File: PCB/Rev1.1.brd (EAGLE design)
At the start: 101.6 x 81.3 mm, 27 parts, among them U1 ATMEGA328P-PU, U2 BT, U3 SMD_H-BRIDGE

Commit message: Minor Board Changes
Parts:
- moved C5 3.81 mm to (71.1, 68.6)
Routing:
- net GND: track 113.1 -> 103.6 mm, vias 14 -> 15
- net 5V: track 151.1 -> 153.7 mm
- net 2.7V: track 41.6 -> 39.6 mm
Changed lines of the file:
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@@
 <element name="C3" library="SparkFun-Capacitors" package="0805" value="2.2uF" x="45.72" y="73.66" rot="R270"/>
 <element name="C4" library="SparkFun-Capacitors" package="0805" value="1uF" x="78.74" y="77.47"/>
-<element name="C5" library="SparkFun-Capacitors" package="0805" value="1uF" x="67.31" y="68.58" rot="R90"/>
+<element name="C5" library="SparkFun-Capacitors" package="0805" value="1uF" x="71.12" y="68.58" rot="R90"/>
 <element name="C6" library="SparkFun-Capacitors" package="0805" value="1uF" x="33.02" y="40.64" rot="R270"/>
 <element name="C7" library="SparkFun-Capacitors" package="0805" value="1uF" x="16.51" y="21.59" rot="R180"/>
@@
 <via x="36.83" y="71.12" extent="1-16" drill="0.6" diameter="0.6096"/>
 <wire x1="36.83" y1="71.12" x2="35.56" y2="71.12" width="0.4064" layer="16"/>
-<wire x1="45.72" y1="74.56" x2="56.78" y2="74.56" width="0.4064" layer="1"/>
 <wire x1="56.78" y1="74.56" x2="57.15" y2="74.93" width="0.4064" layer="1"/>
 <wire x1="57.15" y1="74.93" x2="58.2" y2="74.93" width="0.4064" layer="1"/>
 <wire x1="58.2" y1="74.93" x2="58.42" y2="74.71" width="0.4064" layer="1"/>
 <wire x1="45.72" y1="65.14" x2="45.72" y2="64.99" width="0.4064" layer="1"/>
-<wire x1="45.72" y1="65.14" x2="46.62" y2="65.14" width="0.4064" layer="1"/>
-<wire x1="46.62" y1="65.14" x2="46.99" y2="64.77" width="0.4064" layer="1"/>
-<via x="46.99" y="64.77" extent="1-16" drill="0.6" diameter="0.6096"/>
-<wire x1="46.99" y1="64.77" x2="48.26" y2="64.77" width="0.4064" layer="16"/>
 <wire x1="45.72" y1="74.56" x2="51.7" y2="74.56" width="0.4064" layer="1"/>
 <wire x1="51.7" y1="74.56" x2="52.07" y2="74.93" width="0.4064" layer="1"/>
 <via x="52.07" y="74.93" extent="1-16" drill="0.6" diameter="0.6096"/>
 <wire x1="52.07" y1="74.93" x2="52.07" y2="76.2" width="0.4064" layer="16"/>
-<wire x1="58.42" y1="6.57" x2="62.01" y2="6.57" width="0.4064" layer="1"/>
-<wire x1="62.01" y1="6.57" x2="62.23" y2="6.35" width="0.4064" layer="1"/>
-<via x="62.23" y="6.35" extent="1-16" drill="0.6" diameter="0.6096"/>
-<wire x1="62.23" y1="6.35" x2="63.5" y2="6.35" width="0.4064" layer="16"/>
 <wire x1="43.18" y1="12.48" x2="44.67" y2="12.48" width="0.4064" layer="1"/>
 <wire x1="44.67" y1="12.48" x2="45.72" y2="11.43" width="0.4064" layer="1"/>
@@
 <via x="16.51" y="27.94" extent="1-16" drill="0.6" diameter="0.6096"/>
 <wire x1="16.51" y1="27.94" x2="7.62" y2="27.94" width="0.4064" layer="16"/>
-<wire x1="21.22" y1="24.13" x2="22.86" y2="21.59" width="0.4064" layer="1"/>
-<via x="22.86" y="21.59" extent="1-16" drill="0.6" diameter="0.6096"/>
-<wire x1="28.31" y1="21.59" x2="22.86" y2="21.59" width="0.4064" layer="1"/>
-<wire x1="17.41" y1="21.59" x2="22.86" y2="21.59" width="0.4064" layer="1"/>
 <wire x1="13.74" y1="17.78" x2="13.22" y2="17.78" width="0.4064" layer="1"/>
 <wire x1="13.22" y1="17.78" x2="12.1" y2="16.66" width="0.4064" layer="1"/>
@@
 <via x="11.43" y="20.32" extent="1-16" drill="0.6" diameter="0.6096"/>
 <wire x1="11.43" y1="20.32" x2="11.43" y2="21.59" width="0.4064" layer="16"/>
-<wire x1="41.69" y1="62.23" x2="42.81" y2="62.23" width="0.4064" layer="1"/>
-<wire x1="42.81" y1="62.23" x2="45.72" y2="65.14" width="0.4064" layer="1"/>
+<wire x1="41.69" y1="62.23" x2="43.18" y2="62.23" width="0.4064" layer="1"/>
 <wire x1="29.21" y1="63.13" x2="30.11" y2="63.13" width="0.4064" layer="1"/>
 <wire x1="30.11" y1="63.13" x2="31.75" y2="64.77" width="0.4064" layer="1"/>
@@
 <via x="67.31" y="77.47" extent="1-16" drill="0.6" diameter="0.6096"/>
 <wire x1="67.31" y1="77.47" x2="68.58" y2="77.47" width="0.4064" layer="16"/>
-<wire x1="67.31" y1="67.68" x2="67.31" y2="66.04" width="0.4064" layer="1"/>
-<via x="67.31" y="66.04" extent="1-16" drill="0.6" diameter="0.6096"/>
-<wire x1="67.31" y1="66.04" x2="68.58" y2="66.04" width="0.4064" layer="16"/>
 <wire x1="75.315" y1="71.385" x2="75.315" y2="70.235" width="0.4064" layer="1"/>
 <wire x1="75.315" y1="70.235" x2="74.93" y2="69.85" width="0.4064" layer="1"/>
@@
 <via x="81.28" y="77.47" extent="1-16" drill="0.6" diameter="0.6096"/>
 <wire x1="81.28" y1="77.47" x2="82.55" y2="77.47" width="0.4064" layer="16"/>
+<wire x1="43.18" y1="62.23" x2="44.45" y2="63.5" width="0.4064" layer="1"/>
+<via x="44.45" y="63.5" extent="1-16" drill="0.6" diameter="0.6096"/>
+<wire x1="44.45" y1="63.5" x2="45.72" y2="63.5" width="0.4064" layer="16"/>
+<wire x1="45.72" y1="65.14" x2="45.72" y2="64.77" width="0.4064" layer="1"/>
+<wire x1="45.72" y1="64.77" x2="44.45" y2="63.5" width="0.4064" layer="1"/>
+<wire x1="21.22" y1="24.13" x2="21.22" y2="22.49" width="0.4064" layer="1"/>
+<wire x1="21.22" y1="22.49" x2="20.32" y2="21.59" width="0.4064" layer="1"/>
+<via x="20.32" y="21.59" extent="1-16" drill="0.6" diameter="0.6096"/>
+<wire x1="20.32" y1="21.59" x2="21.59" y2="21.59" width="0.4064" layer="16"/>
+<wire x1="17.41" y1="21.59" x2="20.32" y2="21.59" width="0.4064" layer="1"/>
+<wire x1="28.31" y1="21.59" x2="24.13" y2="21.59" width="0.4064" layer="1"/>
+<via x="24.13" y="21.59" extent="1-16" drill="0.6" diameter="0.6096"/>
+<wire x1="24.13" y1="21.59" x2="22.86" y2="21.59" width="0.4064" layer="16"/>
+<wire x1="58.42" y1="6.57" x2="62.01" y2="6.57" width="0.8128" layer="1"/>
+<wire x1="62.01" y1="6.57" x2="62.23" y2="6.35" width="0.8128" layer="1"/>
+<via x="62.23" y="6.35" extent="1-16" drill="0.6" diameter="0.6096"/>
+<wire x1="62.23" y1="6.35" x2="63.5" y2="6.35" width="0.8128" layer="16"/>
+<wire x1="56.78" y1="74.56" x2="52.44" y2="74.56" width="0.8128" layer="1"/>
+<wire x1="52.44" y1="74.56" x2="52.07" y2="74.93" width="0.8128" layer="1"/>
+<wire x1="71.12" y1="67.68" x2="71.12" y2="67.31" width="0.4064" layer="1"/>
+<wire x1="71.12" y1="67.31" x2="70.485" y2="66.675" width="0.4064" layer="1"/>
+<via x="70.485" y="66.675" extent="1-16" drill="0.6" diameter="0.6096"/>
+<wire x1="70.485" y1="66.675" x2="69.85" y2="66.04" width="0.4064" layer="16"/>
 </signal>
 <signal name="N$1" class="1">
@@
 <wire x1="77.47" y1="77.47" x2="76.85" y2="77.47" width="0.4064" layer="1"/>
 <wire x1="76.85" y1="77.47" x2="75.315" y2="75.935" width="0.4064" layer="1"/>
+<wire x1="44.45" y1="39.37" x2="44.45" y2="36.83" width="0.4064" layer="1"/>
 <wire x1="29.21" y1="60.96" x2="29.21" y2="61.33" width="0" layer="19" extent="1-1"/>
-<wire x1="44.45" y1="36.83" x2="44.45" y2="39.37" width="0" layer="19" extent="1-1"/>
 </signal>
 <signal name="3.3V" class="1">
@@
 <wire x1="69.465" y1="72.685" x2="70.825" y2="72.685" width="0.4064" layer="1"/>
 <wire x1="70.825" y1="72.685" x2="71.12" y2="72.39" width="0.4064" layer="1"/>
-<wire x1="71.12" y1="72.39" x2="71.12" y2="69.85" width="0.4064" layer="1"/>
-<wire x1="71.12" y1="69.85" x2="67.68" y2="69.85" width="0.4064" layer="1"/>
-<wire x1="67.68" y1="69.85" x2="67.31" y2="69.48" width="0.4064" layer="1"/>
 <wire x1="45.72" y1="70.75" x2="47.36" y2="70.75" width="0.4064" layer="1"/>
 <wire x1="47.36" y1="70.75" x2="48.26" y2="69.85" width="0.4064" layer="1"/>
@@
 <via x="68.58" y="68.58" extent="1-16" drill="0.6" diameter="0.6096"/>
 <wire x1="68.58" y1="68.58" x2="68.21" y2="68.58" width="0.4064" layer="1"/>
-<wire x1="68.21" y1="68.58" x2="67.31" y2="69.48" width="0.4064" layer="1"/>
+<wire x1="71.12" y1="69.48" x2="71.12" y2="72.39" width="0.4064" layer="1"/>
+<wire x1="68.58" y1="68.58" x2="70.22" y2="68.58" width="0.4064" layer="1"/>
+<wire x1="70.22" y1="68.58" x2="71.12" y2="69.48" width="0.4064" layer="1"/>
 </signal>
 <signal name="N$3" class="1">

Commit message: Clearance Hotfix
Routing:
- net GND: track 103.6 -> 105.9 mm
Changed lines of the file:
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@@
 <wire x1="52.44" y1="74.56" x2="52.07" y2="74.93" width="0.8128" layer="1"/>
 <wire x1="71.12" y1="67.68" x2="71.12" y2="67.31" width="0.4064" layer="1"/>
-<wire x1="71.12" y1="67.31" x2="70.485" y2="66.675" width="0.4064" layer="1"/>
-<via x="70.485" y="66.675" extent="1-16" drill="0.6" diameter="0.6096"/>
-<wire x1="70.485" y1="66.675" x2="69.85" y2="66.04" width="0.4064" layer="16"/>
+<wire x1="71.12" y1="67.31" x2="68.58" y2="66.04" width="0.4064" layer="1"/>
+<via x="68.58" y="66.04" extent="1-16" drill="0.6" diameter="0.6096"/>
+<wire x1="68.58" y1="66.04" x2="69.85" y2="66.04" width="0.4064" layer="16"/>
 </signal>
 <signal name="N$1" class="1">

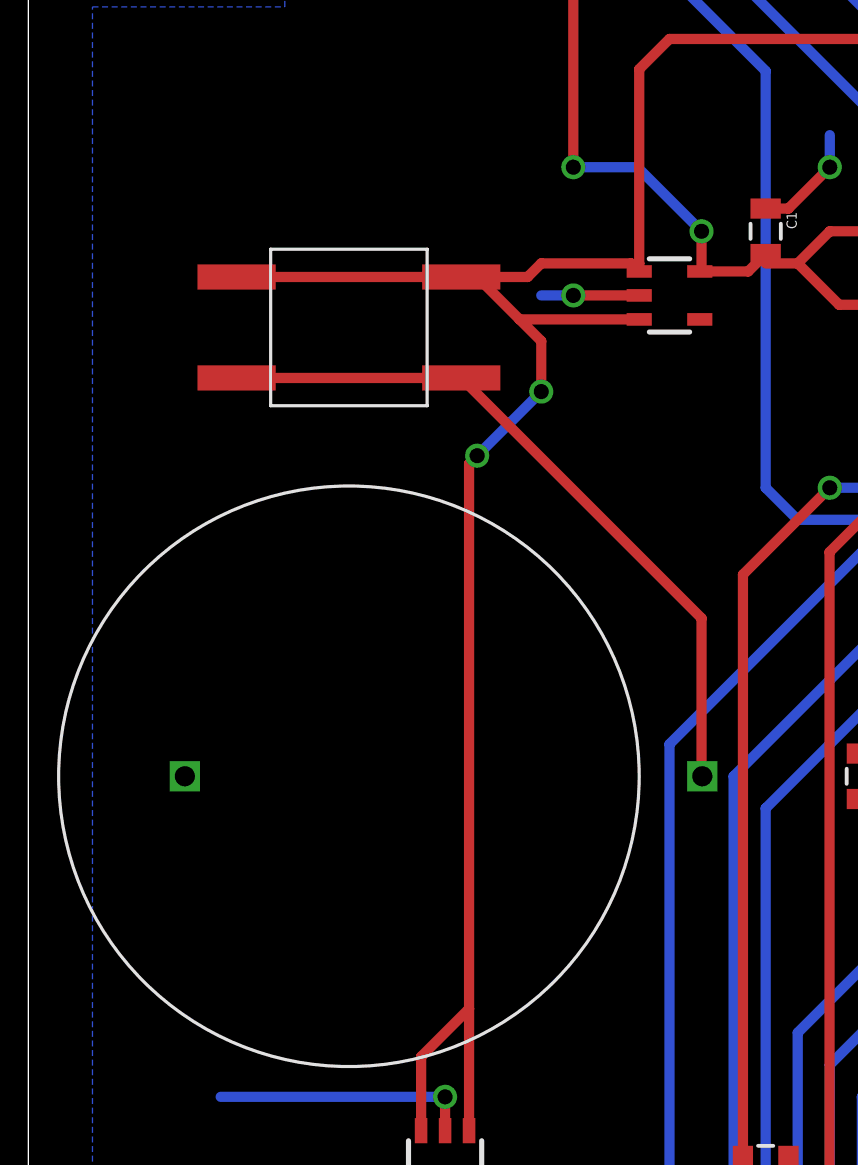
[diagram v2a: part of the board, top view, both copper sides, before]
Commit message: Moved power button to better location.
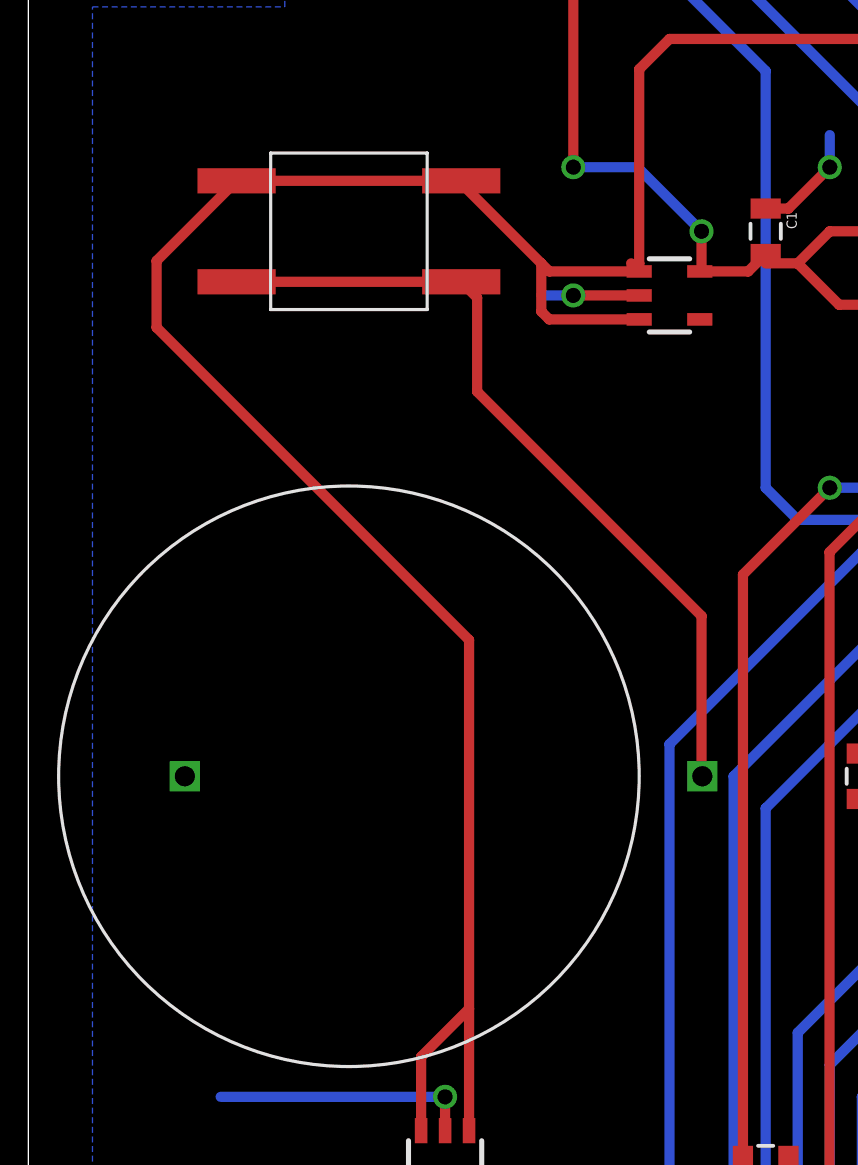
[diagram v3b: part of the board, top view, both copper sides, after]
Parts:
- moved U$2 3.81 mm to (12.7, 62.2)
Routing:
- net N$2: track 94.4 -> 105.2 mm, vias 2 -> 0
- net N$1: track 28.7 -> 32.5 mm
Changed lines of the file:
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@@
 <element name="U2" library="BayouBot" package="BTM400_6B" value="BT" x="25.4" y="11.43" rot="R270"/>
 <element name="U3" library="BayouBot" package="SSOP16" value="SMD_H-BRIDGE" x="72.39" y="73.66" smashed="yes" rot="R270"/>
-<element name="U$2" library="BayouBot" package="POWER_BTN" value="POWER_BTN" x="12.7" y="58.42" rot="R180"/>
+<element name="U$2" library="BayouBot" package="POWER_BTN" value="POWER_BTN" x="12.7" y="62.23" rot="R180"/>
 </elements>
 <signals>
@@
 <contactref element="U$2" pad="P$2"/>
 <wire x1="26.7" y1="40.64" x2="26.67" y2="40.64" width="0.4064" layer="1"/>
-<wire x1="17.15" y1="56.515" x2="17.15" y2="56.42" width="0.4064" layer="1"/>
-<wire x1="17.15" y1="56.42" x2="8.25" y2="56.42" width="0.4064" layer="1"/>
-<wire x1="26.67" y1="40.64" x2="26.67" y2="46.9" width="0.4064" layer="1"/>
-<wire x1="26.67" y1="46.9" x2="17.15" y2="56.42" width="0.4064" layer="1"/>
+<wire x1="17.15" y1="60.23" x2="8.25" y2="60.23" width="0.4064" layer="1"/>
+<wire x1="26.67" y1="40.64" x2="26.67" y2="46.99" width="0.4064" layer="1"/>
+<wire x1="26.67" y1="46.99" x2="17.78" y2="55.88" width="0.4064" layer="1"/>
+<wire x1="17.78" y1="55.88" x2="17.78" y2="59.6" width="0.4064" layer="1"/>
+<wire x1="17.78" y1="59.6" x2="17.15" y2="60.23" width="0.4064" layer="1"/>
 </signal>
 <signal name="N$2" class="1">
@@
 <contactref element="U$2" pad="P$3"/>
 <contactref element="U$2" pad="P$4"/>
-<wire x1="8.25" y1="60.42" x2="17.15" y2="60.42" width="0.4064" layer="1"/>
+<wire x1="8.25" y1="64.23" x2="17.15" y2="64.23" width="0.4064" layer="1"/>
 <wire x1="24.13" y1="60.96" x2="24.2" y2="60.96" width="0.4064" layer="1"/>
 <wire x1="24.2" y1="60.96" x2="24.2" y2="60.64" width="0.4064" layer="1"/>
@@
 <wire x1="39.44" y1="72.07" x2="35.24" y2="72.07" width="0.4064" layer="1"/>
 <wire x1="35.24" y1="72.07" x2="33.02" y2="69.85" width="0.4064" layer="1"/>
-<wire x1="17.15" y1="60.42" x2="17.78" y2="60.42" width="0.4064" layer="1"/>
-<wire x1="17.78" y1="60.42" x2="19.78" y2="60.42" width="0.4064" layer="1"/>
-<wire x1="19.78" y1="60.42" x2="20.32" y2="60.96" width="0.4064" layer="1"/>
-<wire x1="20.32" y1="60.96" x2="23.88" y2="60.96" width="0.4064" layer="1"/>
 <wire x1="23.88" y1="60.96" x2="24.2" y2="60.64" width="0.4064" layer="1"/>
-<wire x1="24.2" y1="58.74" x2="19.46" y2="58.74" width="0.4064" layer="1"/>
-<wire x1="19.46" y1="58.74" x2="17.78" y2="60.42" width="0.4064" layer="1"/>
 <wire x1="15.56" y1="26.6" x2="15.56" y2="29.53" width="0.4064" layer="1"/>
 <wire x1="15.56" y1="29.53" x2="17.46" y2="31.43" width="0.4064" layer="1"/>
 <wire x1="17.46" y1="26.6" x2="17.46" y2="31.43" width="0.4064" layer="1"/>
-<wire x1="17.46" y1="31.43" x2="17.46" y2="53.02" width="0.4064" layer="1"/>
-<wire x1="17.46" y1="53.02" x2="17.78" y2="53.34" width="0.4064" layer="1"/>
-<via x="17.78" y="53.34" extent="1-16" drill="0.6" diameter="0.6096"/>
-<wire x1="17.78" y1="53.34" x2="20.32" y2="55.88" width="0.4064" layer="16"/>
-<via x="20.32" y="55.88" extent="1-16" drill="0.6" diameter="0.6096"/>
-<wire x1="20.32" y1="55.88" x2="20.32" y2="57.88" width="0.4064" layer="1"/>
-<wire x1="20.32" y1="57.88" x2="19.46" y2="58.74" width="0.4064" layer="1"/>
+<wire x1="17.15" y1="64.23" x2="17.15" y2="64.13" width="0.4064" layer="1"/>
+<wire x1="17.15" y1="64.13" x2="20.32" y2="60.96" width="0.4064" layer="1"/>
+<wire x1="20.32" y1="60.96" x2="20.32" y2="59.055" width="0.4064" layer="1"/>
+<wire x1="24.13" y1="60.64" x2="20.64" y2="60.64" width="0.4064" layer="1"/>
+<wire x1="20.64" y1="60.64" x2="20.32" y2="60.96" width="0.4064" layer="1"/>
+<wire x1="24.2" y1="58.74" x2="20.635" y2="58.74" width="0.4064" layer="1"/>
+<wire x1="20.635" y1="58.74" x2="20.32" y2="59.055" width="0.4064" layer="1"/>
+<wire x1="17.46" y1="31.43" x2="17.46" y2="46.04" width="0.4064" layer="1"/>
+<wire x1="17.46" y1="46.04" x2="5.08" y2="58.42" width="0.4064" layer="1"/>
+<wire x1="5.08" y1="58.42" x2="5.08" y2="61.06" width="0.4064" layer="1"/>
+<wire x1="5.08" y1="61.06" x2="8.25" y2="64.23" width="0.4064" layer="1"/>
 </signal>
 <signal name="5V" class="1">
